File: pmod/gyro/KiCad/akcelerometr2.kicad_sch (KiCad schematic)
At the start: 5 parts, among them J2 Conn_01x04_Pin, J3 Conn_01x04_Pin, J4 Conn_01x08_Pin

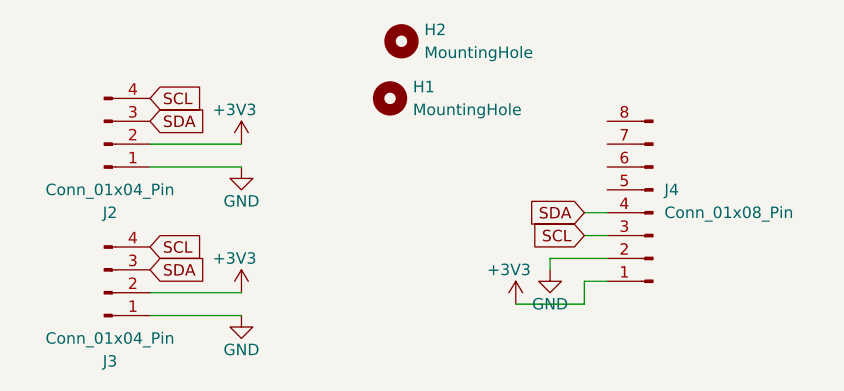
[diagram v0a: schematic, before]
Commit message: fix: prepare all board for manufacturing
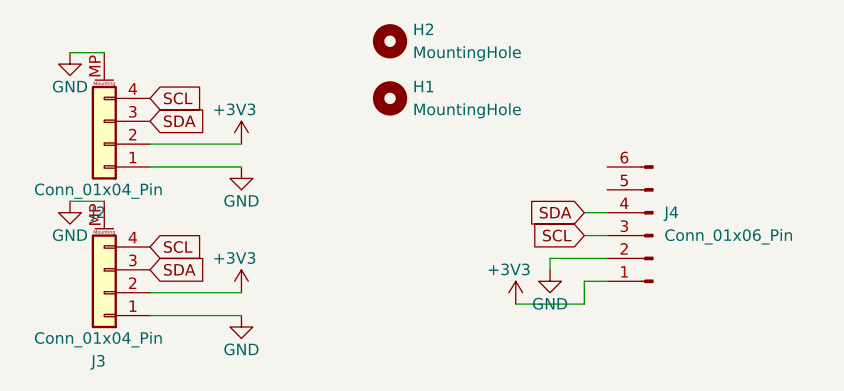
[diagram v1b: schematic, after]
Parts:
- removed J4: Conn_01x08_Pin, Connector_PinHeader_2.54mm:PinHeader_1x08_P2.54mm_Horizontal, symbol Connector:Conn_01x08_Pin
- added J4: Conn_01x06_Pin, Connector_PinHeader_2.54mm:PinHeader_1x06_P2.54mm_Horizontal, symbol Connector:Conn_01x06_Pin
- J2, J3: symbol Connector:Conn_01x04_Pin -> Connector_Generic_MountingPin:Conn_01x04_MountingPin
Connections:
- net +3V3: now also J4.1 (Pin_1)
- net GND: now also J2.MP (MountPin), J3.MP (MountPin), J4.2 (Pin_2)
- net SCL: now also J4.3 (Pin_3)
- net SDA: now also J4.4 (Pin_4)
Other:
- moved on the sheet: H2

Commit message: docs: add images, fix docs
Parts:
- removed J4: Conn_01x06_Pin, Connector_PinHeader_2.54mm:PinHeader_1x06_P2.54mm_Horizontal, symbol Connector:Conn_01x06_Pin
- added J4: Conn_01x06_Pin, Connector_PinHeader_2.54mm:PinHeader_1x08_P2.54mm_Vertical, symbol Connector:Conn_01x08_Pin
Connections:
- net +3V3: now also J4.1 (Pin_1)
- net GND: now also J4.2 (Pin_2)
- net SCL: now also J4.3 (Pin_3)
- net SDA: now also J4.4 (Pin_4)
- no-connect marks 0 -> 4
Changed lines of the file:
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@@
 	(generator_version "10.0")
 	(paper "A4")
+	(no_connect
+		(at 167.64 68.58)
+	)
+	(no_connect
+		(at 167.64 66.04)
+	)
+	(no_connect
+		(at 167.64 73.66)
+	)
+	(no_connect
+		(at 167.64 71.12)
+	)
 	(wire
 		(pts
@@
 	)
 	(symbol
-		(lib_id "Connector:Conn_01x06_Pin")
-		(at 172.72 78.74 180)
-		(unit 1)
-		(body_style 1)
-		(exclude_from_sim no)
-		(in_bom yes)
-		(on_board yes)
-		(in_pos_files yes)
-		(dnp no)
-		(fields_autoplaced yes)
-		(property "Reference" "J4"
-			(at 173.99 76.1999 0)
-			(show_name no)
-			(do_not_autoplace no)
-			(effects
-				(font
-					(size 1.27 1.27)
-				)
-				(justify right)
-			)
-		)
-		(property "Value" "Conn_01x06_Pin"
-			(at 173.99 78.7399 0)
-			(show_name no)
-			(do_not_autoplace no)
-			(effects
-				(font
-					(size 1.27 1.27)
-				)
-				(justify right)
-			)
-		)
-		(property "Footprint" "Connector_PinHeader_2.54mm:PinHeader_1x06_P2.54mm_Horizontal"
-			(at 172.72 78.74 0)
-			(hide yes)
-			(show_name no)
-			(do_not_autoplace no)
-			(effects
-				(font
-					(size 1.27 1.27)
-				)
-			)
-		)
-		(property "Datasheet" ""
-			(at 172.72 78.74 0)
-			(hide yes)
-			(show_name no)
-			(do_not_autoplace no)
-			(effects
-				(font
-					(size 1.27 1.27)
-				)
-			)
-		)
-		(property "Description" "Generic connector, single row, 01x06, script generated"
-			(at 172.72 78.74 0)
-			(hide yes)
-			(show_name no)
-			(do_not_autoplace no)
-			(effects
-				(font
-					(size 1.27 1.27)
-				)
-			)
-		)
-		(pin "4"
-		)
-		(pin "3"
-		)
-		(pin "1"
-		)
-		(pin "2"
-		)
-		(pin "5"
-		)
-		(pin "6"
-		)
-		(instances
-			(project "akcelerometr2"
-				(path "/3ee8cf12-798b-4a99-8d39-0f2ac3c6d2d6"
-					(reference "J4")
-					(unit 1)
-				)
-			)
-		)
-	)
-	(symbol
 		(lib_id "power:GND")
 		(at 161.29 82.55 0)
@@
 					(unit 1)
 				)
+			)
+		)
+	)
+	(symbol
+		(lib_id "Connector:Conn_01x08_Pin")
+		(at 172.72 76.2 180)
+		(unit 1)
+		(body_style 1)
+		(exclude_from_sim no)
+		(in_bom yes)
+		(on_board yes)
+		(in_pos_files yes)
+		(dnp no)
+		(fields_autoplaced yes)
+		(property "Reference" "J4"
+			(at 173.99 73.6599 0)
+			(show_name no)
+			(do_not_autoplace no)
+			(effects
+				(font
+					(size 1.27 1.27)
+				)
+				(justify right)
+			)
+		)
+		(property "Value" "Conn_01x06_Pin"
+			(at 173.99 76.1999 0)
+			(show_name no)
+			(do_not_autoplace no)
+			(effects
+				(font
+					(size 1.27 1.27)
+				)
+				(justify right)
+			)
+		)
+		(property "Footprint" "Connector_PinHeader_2.54mm:PinHeader_1x08_P2.54mm_Vertical"
+			(at 172.72 76.2 0)
+			(hide yes)
+			(show_name no)
+			(do_not_autoplace no)
+			(effects
+				(font
+					(size 1.27 1.27)
+				)
+			)
+		)
+		(property "Datasheet" ""
+			(at 172.72 76.2 0)
+			(hide yes)
+			(show_name no)
+			(do_not_autoplace no)
+			(effects
+				(font
+					(size 1.27 1.27)
+				)
+			)
+		)
+		(property "Description" "Generic connector, single row, 01x08, script generated"
+			(at 172.72 76.2 0)
+			(hide yes)
+			(show_name no)
+			(do_not_autoplace no)
+			(effects
+				(font
+					(size 1.27 1.27)
+				)
+			)
+		)
+		(pin "4"
+		)
+		(pin "3"
+		)
+		(pin "1"
+		)
+		(pin "2"
+		)
+		(pin "5"
+		)
+		(pin "6"
+		)
+		(pin "7"
+		)
+		(pin "8"
+		)
+		(instances
+			(project "akcelerometr2"
+				(path "/3ee8cf12-798b-4a99-8d39-0f2ac3c6d2d6"
+					(reference "J4")
+					(unit 1)
+				)
